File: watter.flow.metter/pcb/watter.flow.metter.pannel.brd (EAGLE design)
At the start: 131.9 x 48.2 mm, 25 parts, among them Q1 BC546A

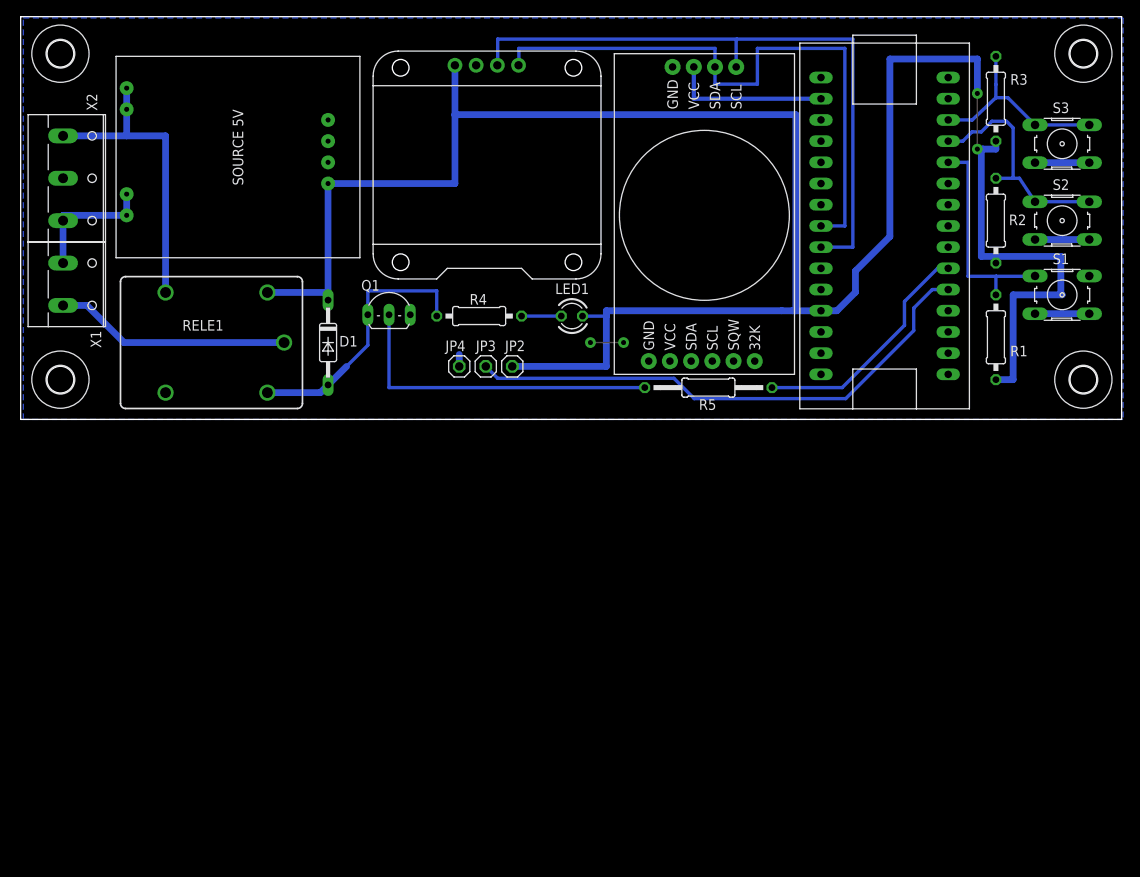
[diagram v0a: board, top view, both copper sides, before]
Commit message: clock with dimmer and date switching
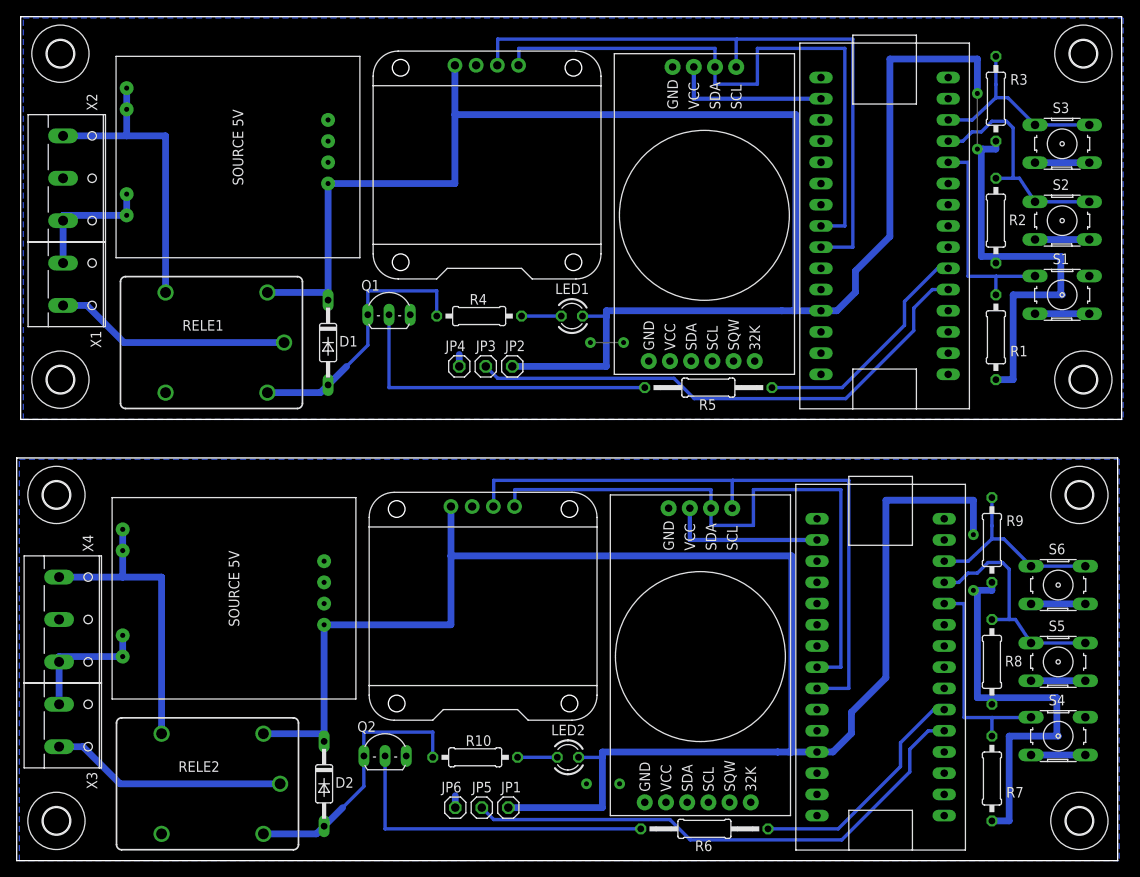
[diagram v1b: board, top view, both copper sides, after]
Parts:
- added D2: 1N4148DO35-10, diode:DO35-10
- added DISPLAY1: OLED_0.96_I2C, tft_1.8_1.44_oled_0.96:OLED_0.96_I2C
- added JP1, JP5, JP6: (no value), pinhead:1X01
- added LED2: (no value), led:LED3MM
- added Q2: BC546A, transistor-npn:TO92-EBC
- added R10, R7, R8, R9: (no value), rcl:0207/10
- added R6: (no value), rcl:0207/15
- added RELE2: JS-M1-9V-4, relay:JS-M
- added S4, S5, S6: (no value), switch-omron:B3F-10XX
- added U$1: NANO, Arduino:NANO
- added U$10: PWR5V, SOURCE:SUPP
- added U$11, U$12, U$13, U$14: (no value), holes:3,2
- added U$9: DS3231BOARD, DS3232M:BOARD
- added X3: (no value), con-wago-508:W237-132
- added X4: (no value), con-wago-508:W237-3E
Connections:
- new net 3.3V1: U$1.3.3V, U$9.VCC@2
- new net D1: JP5.1, U$1.D2
- new net D4: R6.1, U$1.D3
- new net GND1: DISPLAY1.GND, JP6.1, Q2.E, S4.3, S4.4, S5.3, S5.4, S6.3, S6.4, U$1.GND, U$10.P$5, U$9.GND@1, U$9.GND@2
- new net N$10: U$10.P$3, U$10.P$4, X3.1, X4.3
- new net N$11: RELE2.NO, U$10.P$1, U$10.P$2, X4.1
- new net N$12: RELE2.C, X3.2
- new net N$13: R7.1, S4.1, S4.2, U$1.D8
- new net N$14: R8.1, S5.1, S5.2, U$1.D9
- new net N$15: R9.1, S6.1, S6.2, U$1.D10
- new net N$16: Q2.B, R6.2
- new net N$17: LED2.K, R10.2
- new net N$9: D2.A, Q2.C, R10.1, RELE2.2
- new net SCL1: DISPLAY1.SCL, U$1.A5, U$9.SCL@2
- new net SDA1: DISPLAY1.SDA, U$1.A4, U$9.SDA@2
- new net VCC1: D2.C, DISPLAY1.VCC, JP1.1, LED2.A, R7.2, R8.2, R9.2, RELE2.1, U$1.5V, U$10.P$8, U$9.VCC@1
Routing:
- net VCC1: track 0.00 -> 261.0 mm, vias 0 -> 2
- net SCL1: track 0.00 -> 77.9 mm
- net SDA1: track 0.00 -> 73.8 mm
- net D1: track 0.00 -> 64.0 mm
- net N$16: track 0.00 -> 39.4 mm
- net N$11: track 0.00 -> 36.8 mm
- net N$9: track 0.00 -> 32.2 mm
- net D4: track 0.00 -> 28.7 mm
- net N$12: track 0.00 -> 28.3 mm
- net N$14: track 0.00 -> 27.9 mm
- net N$13: track 0.00 -> 26.3 mm
- net N$15: track 0.00 -> 24.3 mm
- net GND1: track 0.00 -> 21.0 mm, vias 0 -> 2
- net 3.3V1: track 0.00 -> 19.0 mm
- net N$10: track 0.00 -> 15.9 mm
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- added copper zone on layer 16, net GND1
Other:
- board size 131.9 x 48.2 mm -> 132.4 x 101.1 mm
